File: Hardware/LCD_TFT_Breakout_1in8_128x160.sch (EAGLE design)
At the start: 34 parts, among them Q1 220mA/50V/3.5Ω, Q2 220mA/50V/3.5Ω, U2 W25Q32FV, U6 TXB0108DQSR, U7 3.3V

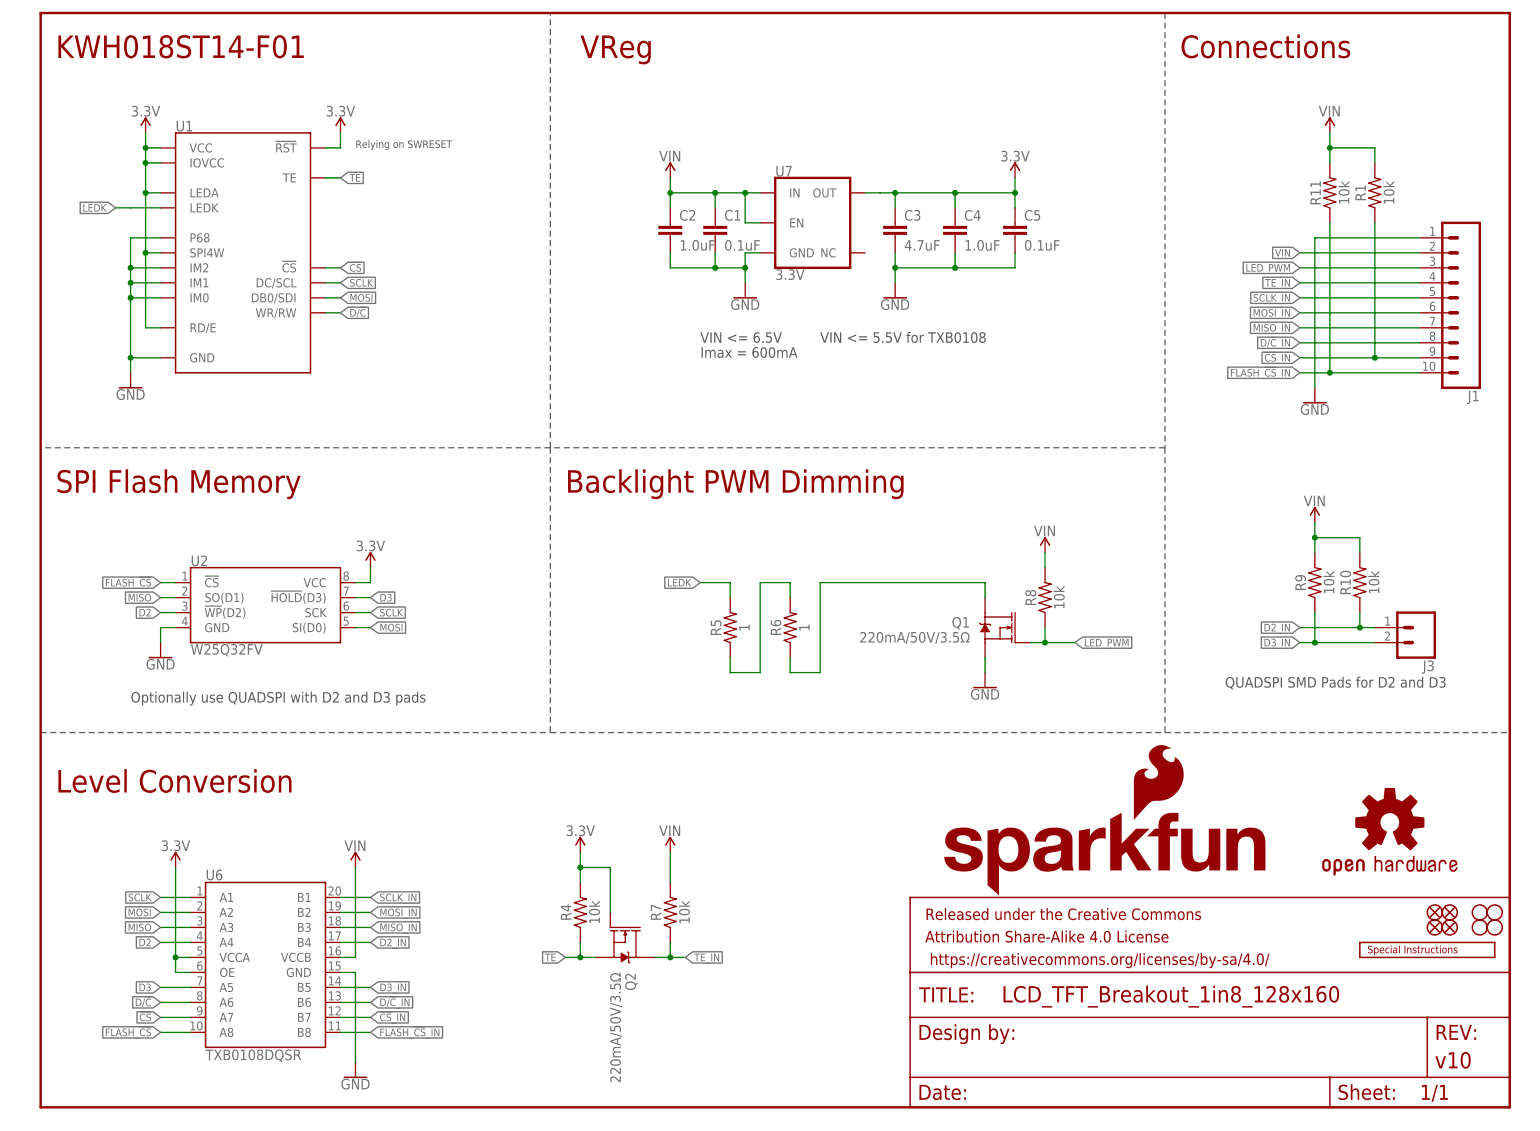
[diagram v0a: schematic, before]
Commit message: Change to SD from SPI flash
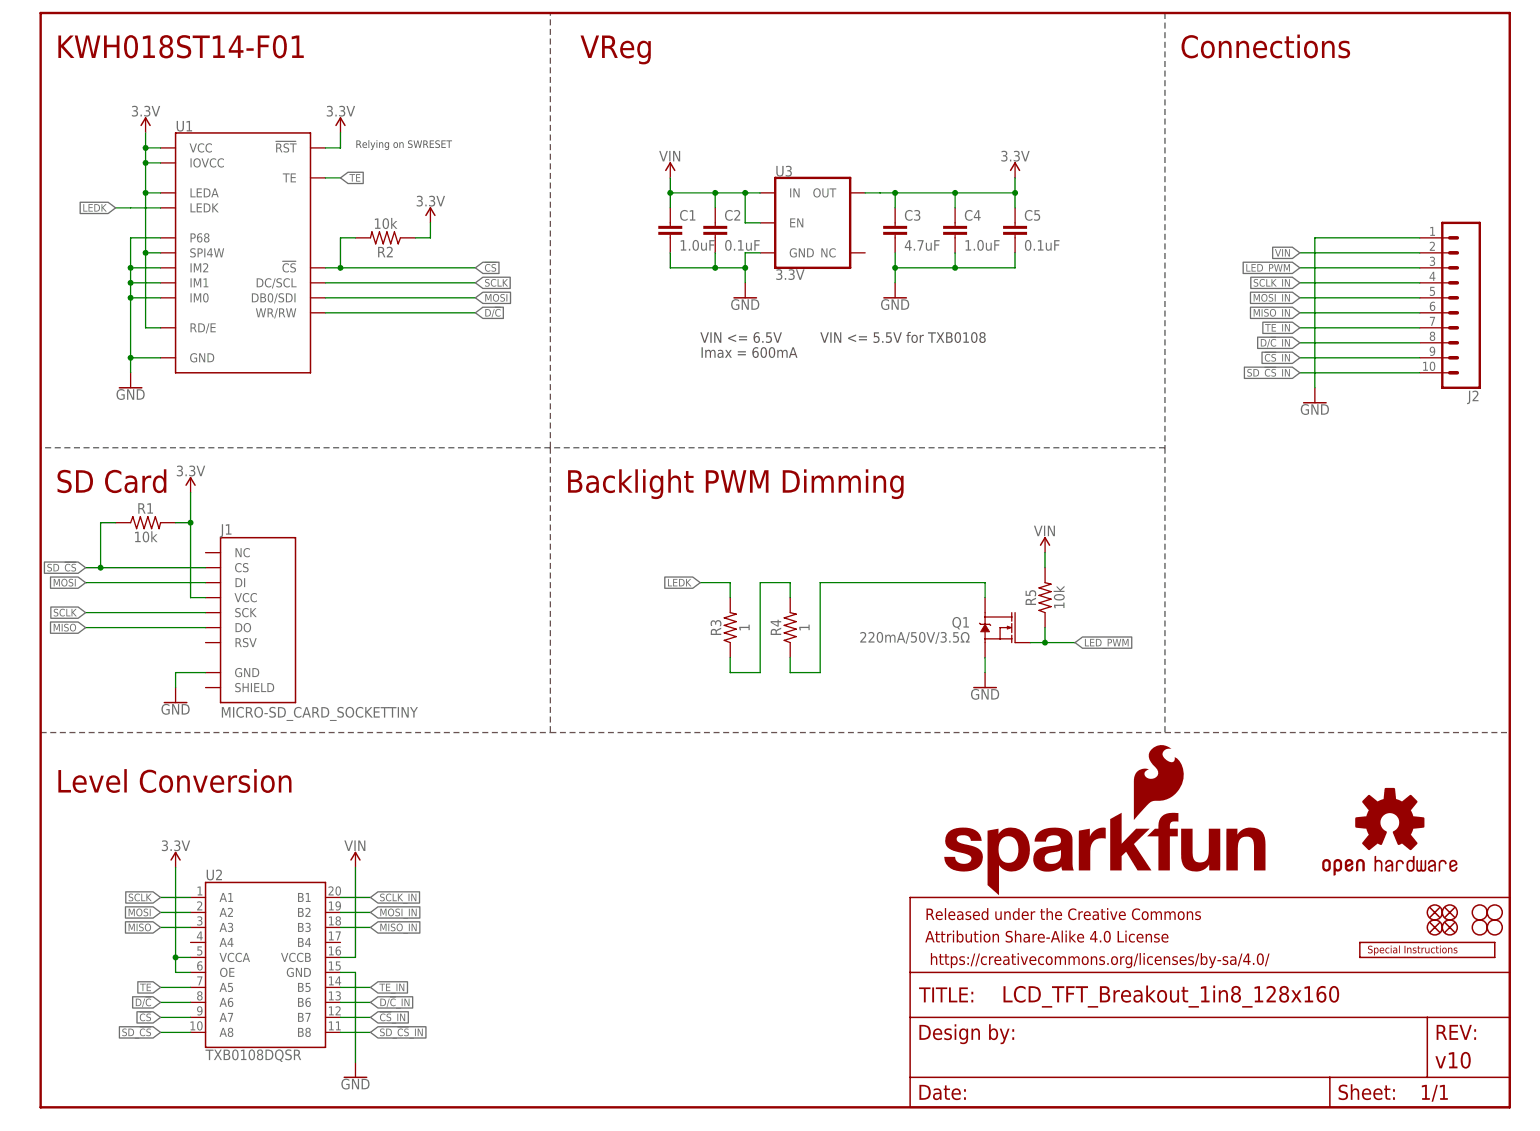
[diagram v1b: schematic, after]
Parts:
- removed J3: (no value), 1in8_breakout:CONN_02-USER_SMD
- removed Q2: 220mA/50V/3.5Ω, SparkFun-DiscreteSemi:MOSFET-NCH-BSS138
- removed R10, R11, R7, R8, R9: 10k, SparkFun-Resistors:10KOHM-0603-1/10W-1%
- removed R6: 1, SparkFun-Resistors:1OHM-0603-1/10W-1%
- removed U$4: SPECIAL_INSTRUCTIONS-PRODUCTION, SparkFun-Aesthetics:SPECIAL_INSTRUCTIONS-PRODUCTION
- removed U6: TXB0108DQSR, SparkFun-IC-Comms:TXB0108
- added J2: (no value), SparkFun-Connectors:CONN_10NO_SILK_PTH_FEMALE
- added LOGO3: OSHW-LOGOS, SparkFun-Aesthetics:OSHW-LOGOS
- added R2: 10k, SparkFun-Resistors:10KOHM-0603-1/10W-1%
- added R3: 1, SparkFun-Resistors:1OHM-0603-1/10W-1%
- C1: value 0.1uF -> 1.0uF; device SparkFun-Capacitors:0.1UF-0603-100V-10% -> SparkFun-Capacitors:1.0UF-0603-16V-10%
- C2: value 1.0uF -> 0.1uF; device SparkFun-Capacitors:1.0UF-0603-16V-10% -> SparkFun-Capacitors:0.1UF-0603-100V-10%
- J1: value (none) -> MICRO-SD_CARD_SOCKETTINY; device SparkFun-Connectors:CONN_10NO_SILK_PTH_FEMALE -> SparkFun-Connectors:MICRO-SD_CARD_SOCKETTINY
- LOGO2: value OSHW-LOGOS -> SPECIAL_INSTRUCTIONS-PRODUCTION; device SparkFun-Aesthetics:OSHW-LOGOS -> SparkFun-Aesthetics:SPECIAL_INSTRUCTIONS-PRODUCTION
- R4: value 10k -> 1; device SparkFun-Resistors:10KOHM-0603-1/10W-1% -> SparkFun-Resistors:1OHM-0603-1/10W-1%
- R5: value 1 -> 10k; device SparkFun-Resistors:1OHM-0603-1/10W-1% -> SparkFun-Resistors:10KOHM-0603-1/10W-1%
- U2: value W25Q32FV -> TXB0108DQSR; device SparkFun-IC-Memory:W25Q32FVSS -> SparkFun-IC-Comms:TXB0108
- renumbered FRAME2 to FRAME1, U7 to U3
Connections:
- removed net D2: U2.!WP!(D2), U6.A4
- removed net D2_IN: J3.1, R10.1, U6.B4
- removed net D3: U2.!HOLD!(D3), U6.A5
- removed net D3_IN: J3.2, R9.1, U6.B5
- removed net FLASH_!CS: U2.!CS!, U6.A8
- removed net FLASH_!CS!_IN: J1.10, R11.1, U6.B8
- new net SD_!CS: J1.CS, R1.1, U2.A8
- new net SD_!CS!_IN: J2.10, U2.B8
- net !CS: now also R2.2, U2.A7; no longer U6.A7
- net !CS!_IN: now also J2.9, U2.B7; no longer J1.9, R1.1, U6.B7
- net 3.3V: now also J1.VCC, R1.2, R2.1, U2.OE, U2.VCCA; no longer Q2.G, R4.2, U2.VCC, U6.OE, U6.VCCA
- net D/!C: now also U2.A6; no longer U6.A6
- net D/!C!_IN: now also J2.8, U2.B6; no longer J1.8, U6.B6
- net GND: now also J1.GND, J2.1; no longer J1.1, U6.GND
- net LEDK: now also R3.2; no longer R5.2
- net LED_PWM: now also J2.3, R5.1; no longer J1.3, R8.1
- net MISO: now also J1.DO, U2.A3; no longer U2.SO(D1), U6.A3
- net MISO_IN: now also J2.6, U2.B3; no longer J1.7, U6.B3
- net MOSI: now also J1.DI, U2.A2; no longer U2.SI(D0), U6.A2
- net MOSI_IN: now also J2.5, U2.B2; no longer J1.6, U6.B2
- net N$4: now also R3.1, R4.2; no longer R5.1, R6.2
- net N$5: now also R4.1; no longer R6.1
- net SCLK: now also J1.SCK, U2.A1; no longer U2.SCK, U6.A1
- net SCLK_IN: now also J2.4, U2.B1; no longer J1.5, U6.B1
- net TE: now also U2.A5; no longer Q2.S, R4.1
- net TE_IN: now also J2.7, U2.B5; no longer J1.4, Q2.D, R7.1
- net VIN: now also J2.2, R5.2, U2.VCCB; no longer J1.2, R1.2, R10.2, R11.2, R7.2, R8.2, R9.2, U6.VCCB
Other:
- note added: "SD Card"
- note removed: "Optionally use QUADSPI with D2 and D3 pads"
- note removed: "QUADSPI SMD Pads for D2 and D3"
- note removed: "SPI Flash Memory"
- moved on the sheet: C1, C2, R1, R4, R5

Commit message: Small fixes/tweaks according to checklist
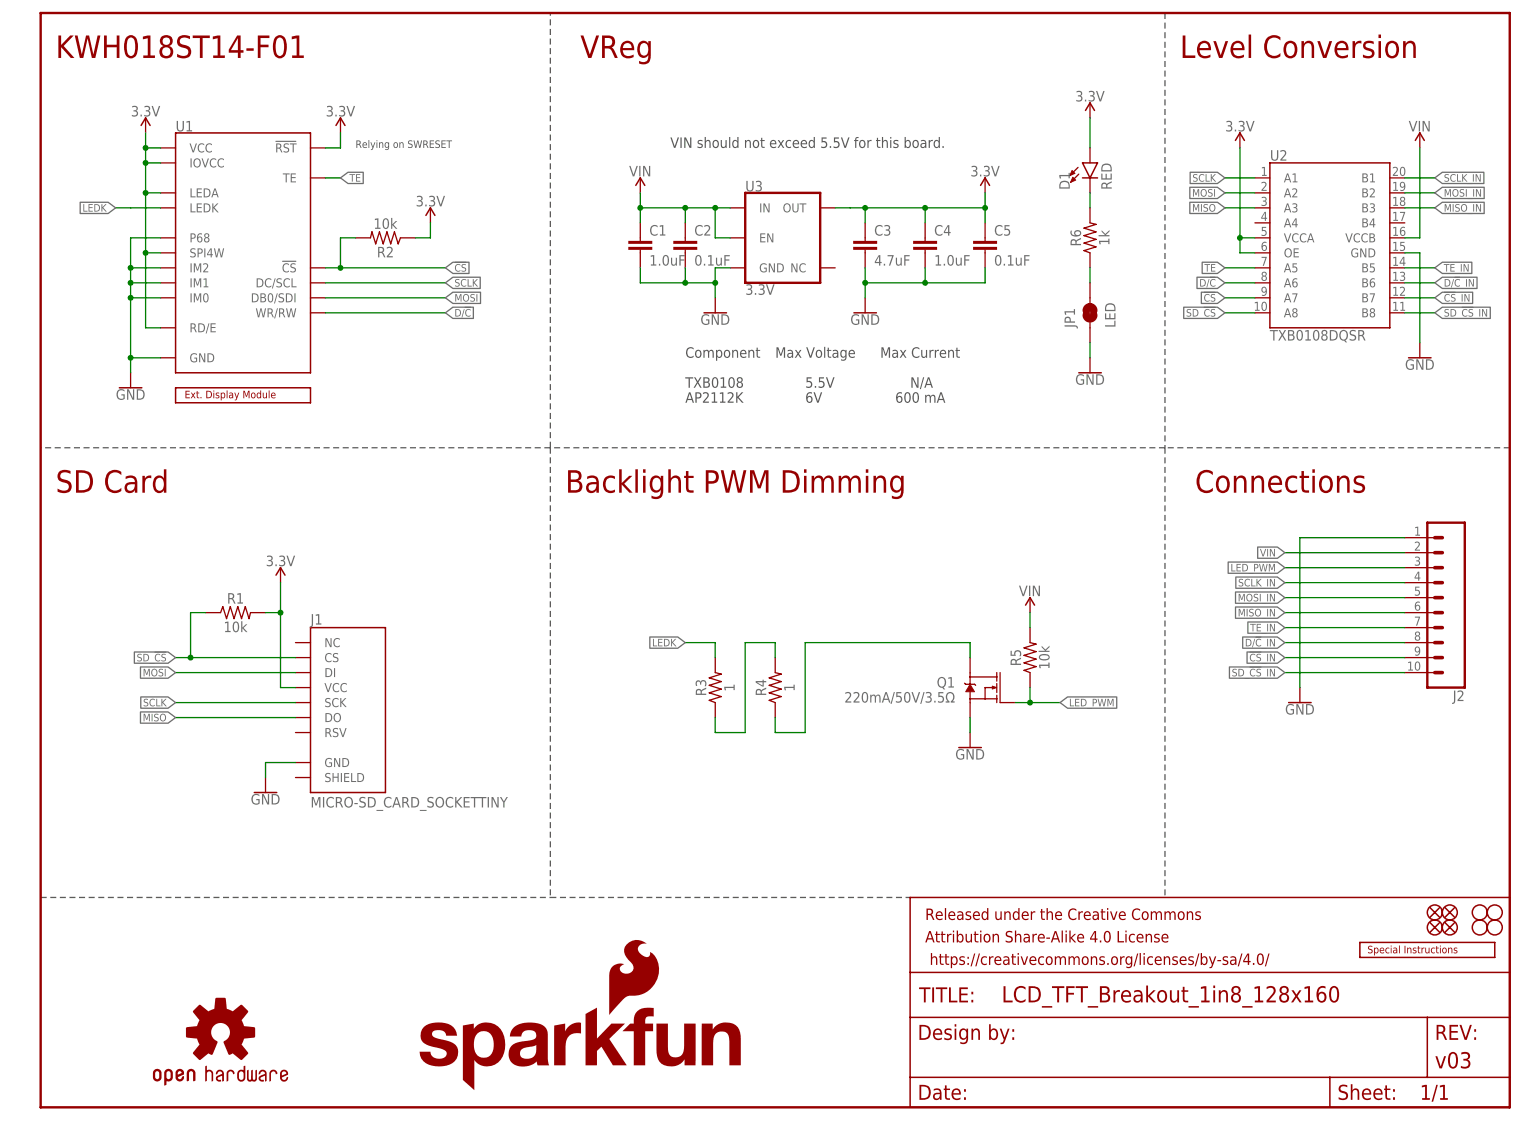
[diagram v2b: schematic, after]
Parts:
- added D1: RED, SparkFun-LED:LED-RED0603
- added JP1: LED, SparkFun-Jumpers:JUMPER-SMT_2_NC_TRACE_SILK
- added R6: 1k, SparkFun-Resistors:1KOHM-0603-1/10W-1%
- added U$33: EXTERNAL_DISP-KWH018ST14-F01, SparkFun-Displays:EXTERNAL_DISP-KWH018ST14-F01
- FRAME1: REV v10 -> v03
- U1: device 1in8_breakout:KWH018ST14-F01_4WSPI-REVERSE -> SparkFun-Displays:KWH018ST14-F01_4WSPI-BOTTOM
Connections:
- new net N$1: D1.C, R6.2
- new net N$2: JP1.2, R6.1
- net 3.3V: now also D1.A
- net GND: now also JP1.1
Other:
- note added: "5.5V"
- note added: "600 mA"
- note added: "6V"
- note added: "AP2112K"
- note added: "Component"
- note added: "Max Current"
- note added: "Max Voltage"
- note added: "N/A"
- note added: "TXB0108"
- note added: "VIN should not exceed 5.5V for this board."
- note removed: "Imax = 600mA"
- note removed: "VIN <= 5.5V for TXB0108"
- note removed: "VIN <= 6.5V"
- moved on the sheet: C1, C2, C3, C4, C5, J1, J2, Q1, R1, R3, R4, R5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

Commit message: Perform Proto Review task items
Completes and closes issue #1
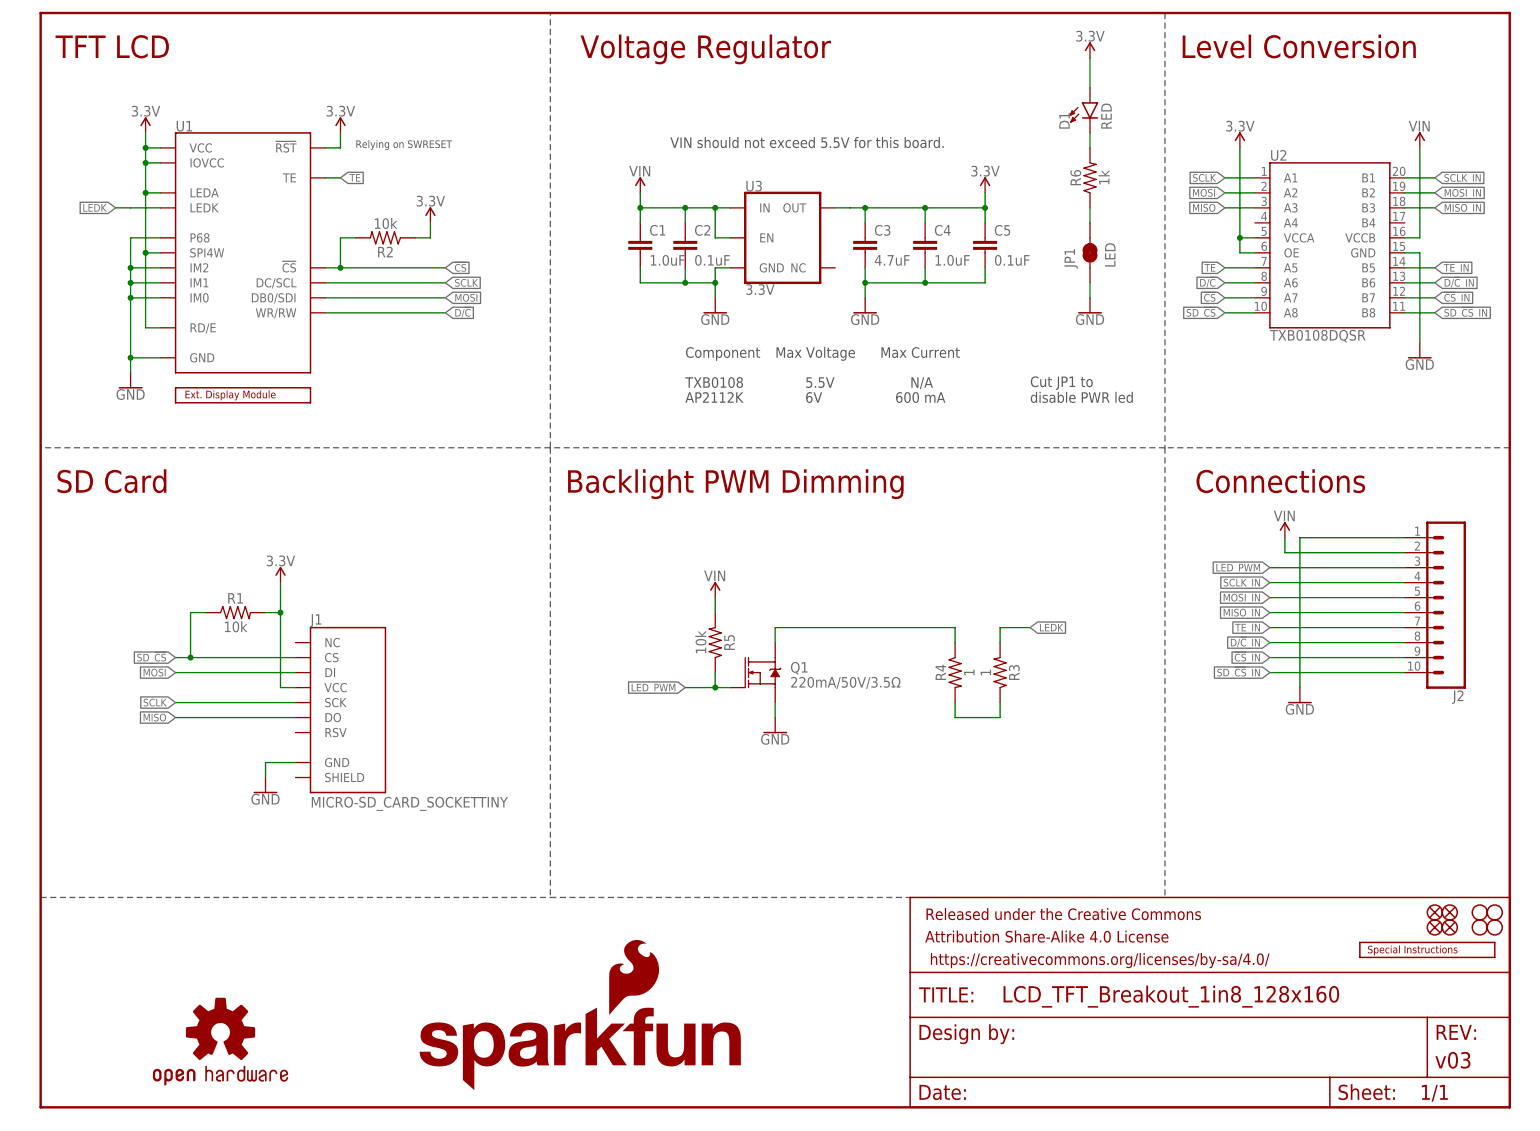
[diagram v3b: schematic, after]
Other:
- note added: "Cut JP1 to disable PWR led"
- note added: "TFT LCD"
- note added: "Voltage Regulator"
- note removed: "KWH018ST14-F01"
- note removed: "VReg"
- moved on the sheet: D1, JP1, Q1, R3, R4, R5, R6

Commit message: Perform checklist after proto review
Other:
- note added: "VIN 3.3V at minimum"
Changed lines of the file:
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@@
 <text x="167.64" y="119.38" size="1.778" layer="97">Cut JP1 to
 disable PWR led</text>
+<text x="106.68" y="160.02" size="1.778" layer="97">VIN 3.3V at minimum</text>
 </plain>
 <instances>

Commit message: Fixed Reds Design Review Issues
As shown in isse #2
- Offset route-out from v-score
- Added FPC numbers in silk

- Additional little silk rearrangements/tweaking
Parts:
- added FD5, FD6: FIDUCIAL1X2, SparkFun-Aesthetics:FIDUCIAL1X2

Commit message: Make output connector look prettier in schematic
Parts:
- removed FD5, FD6: FIDUCIAL1X2, SparkFun-Aesthetics:FIDUCIAL1X2
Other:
- moved on the sheet: J2

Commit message: Update version to v10
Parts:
- FRAME1: REV v03 -> v10
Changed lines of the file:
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@@
 <part name="FRAME1" library="SparkFun-Aesthetics" deviceset="FRAME-LETTER" device="">
 <attribute name="DESIGNER" value="Owen Lyke"/>
-<attribute name="REV" value="v03"/>
+<attribute name="REV" value="v10"/>
 </part>
 <part name="U2" library="SparkFun-IC-Comms" deviceset="TXB0108" device="" value="TXB0108DQSR"/>
